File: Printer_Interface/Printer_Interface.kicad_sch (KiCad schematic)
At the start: 0 parts

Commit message: Finished schematic, review time...
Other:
- added sheet Interrupt logic (interrupt.kicad_sch)
- added sheet Printer port (printer_port.kicad_sch)
- added sheet Registers (registers.kicad_sch)
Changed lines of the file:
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@@
   (title_block
     (title "PARALLEL PRINTER INTERFACE")
-    (date "2024-02-20")
+    (date "2024-02-21")
     (rev "1")
     (company "(C) TOM STOREY")
@@
     )
   )
+  (sheet (at 193.04 35.56) (size 30.48 17.78) (fields_autoplaced)
+    (stroke (width 0.1524) (type solid))
+    (fill (color 0 0 0 0.0000))
+    (property "Sheetname" "Interrupt logic" (at 193.04 34.8484 0)
+      (effects (font (size 1.27 1.27)) (justify left bottom))
+    )
+    (property "Sheetfile" "interrupt.kicad_sch" (at 193.04 53.9246 0)
+      (effects (font (size 1.27 1.27)) (justify left top))
+    )
+    (instances
+      (project "Printer_Interface"
+        (path "/75b66dbb-7202-4875-8695-2c14dee692f0" (page "6"))
+      )
+    )
+  )
   (sheet (at 154.94 35.56) (size 30.48 17.78) (fields_autoplaced)
     (stroke (width 0.1524) (type solid))
@@
       (project "Printer_Interface"
         (path "/75b66dbb-7202-4875-8695-2c14dee692f0" (page "5"))
+      )
+    )
+  )
+  (sheet (at 40.64 66.04) (size 30.48 17.78) (fields_autoplaced)
+    (stroke (width 0.1524) (type solid))
+    (fill (color 0 0 0 0.0000))
+    (property "Sheetname" "Registers" (at 40.64 65.3284 0)
+      (effects (font (size 1.27 1.27)) (justify left bottom))
+    )
+    (property "Sheetfile" "registers.kicad_sch" (at 40.64 84.4046 0)
+      (effects (font (size 1.27 1.27)) (justify left top))
+    )
+    (instances
+      (project "Printer_Interface"
+        (path "/75b66dbb-7202-4875-8695-2c14dee692f0" (page "7"))
       )
     )
@@
       )
     )
+  )
+  (sheet (at 78.74 66.04) (size 30.48 17.78) (fields_autoplaced)
+    (stroke (width 0.1524) (type solid))
+    (fill (color 0 0 0 0.0000))
+    (property "Sheetname" "Printer port" (at 78.74 65.3284 0)
+      (effects (font (size 1.27 1.27)) (justify left bottom))
+    )
+    (property "Sheetfile" "printer_port.kicad_sch" (at 78.74 84.4046 0)
+      (effects (font (size 1.27 1.27)) (justify left top))
+    )
+    (instances
+      (project "Printer_Interface"
+        (path "/75b66dbb-7202-4875-8695-2c14dee692f0" (page "8"))
+      )
+    )

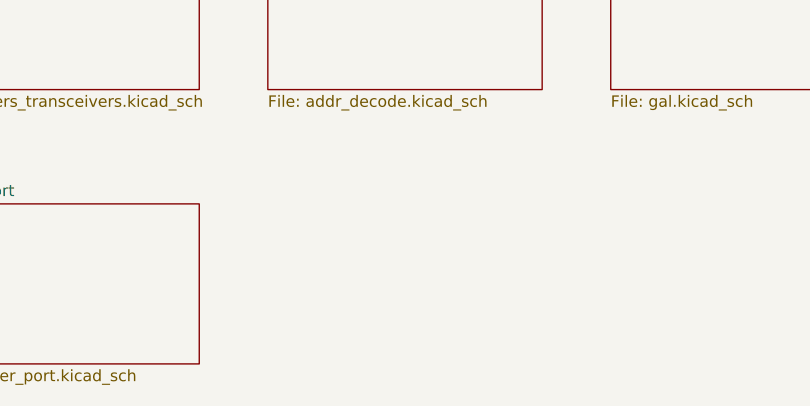
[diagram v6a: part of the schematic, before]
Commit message: Add register documentation sheet
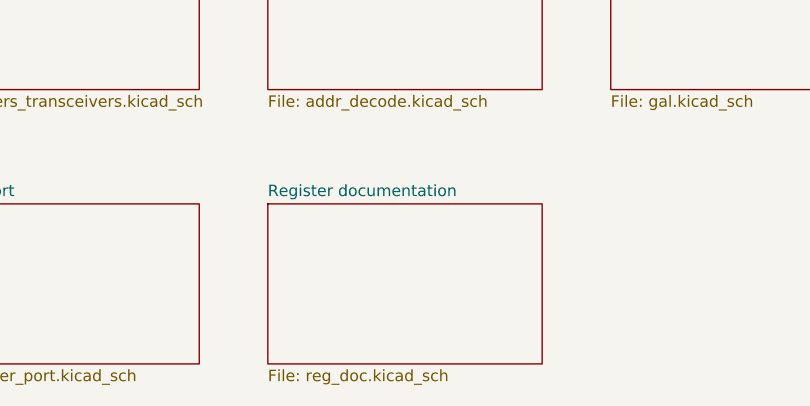
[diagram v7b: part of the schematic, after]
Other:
- added sheet Register documentation (reg_doc.kicad_sch)
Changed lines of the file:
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@@
+	)
+	(sheet
+		(at 116.84 66.04)
+		(size 30.48 17.78)
+		(fields_autoplaced yes)
+		(stroke
+			(width 0.1524)
+			(type solid)
+		)
+		(fill
+			(color 0 0 0 0.0000)
+		)
+		(property "Sheetname" "Register documentation"
+			(at 116.84 65.3284 0)
+			(effects
+				(font
+					(size 1.27 1.27)
+				)
+				(justify left bottom)
+			)
+		)
+		(property "Sheetfile" "reg_doc.kicad_sch"
+			(at 116.84 84.4046 0)
+			(effects
+				(font
+					(size 1.27 1.27)
+				)
+				(justify left top)
+			)
+		)
+		(instances
+			(project "Printer_Interface"
+				(path "/75b66dbb-7202-4875-8695-2c14dee692f0"
+					(page "9")
+				)
+			)
+		)
 	)
 	(sheet
